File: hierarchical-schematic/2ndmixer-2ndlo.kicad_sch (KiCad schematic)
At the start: 58 parts

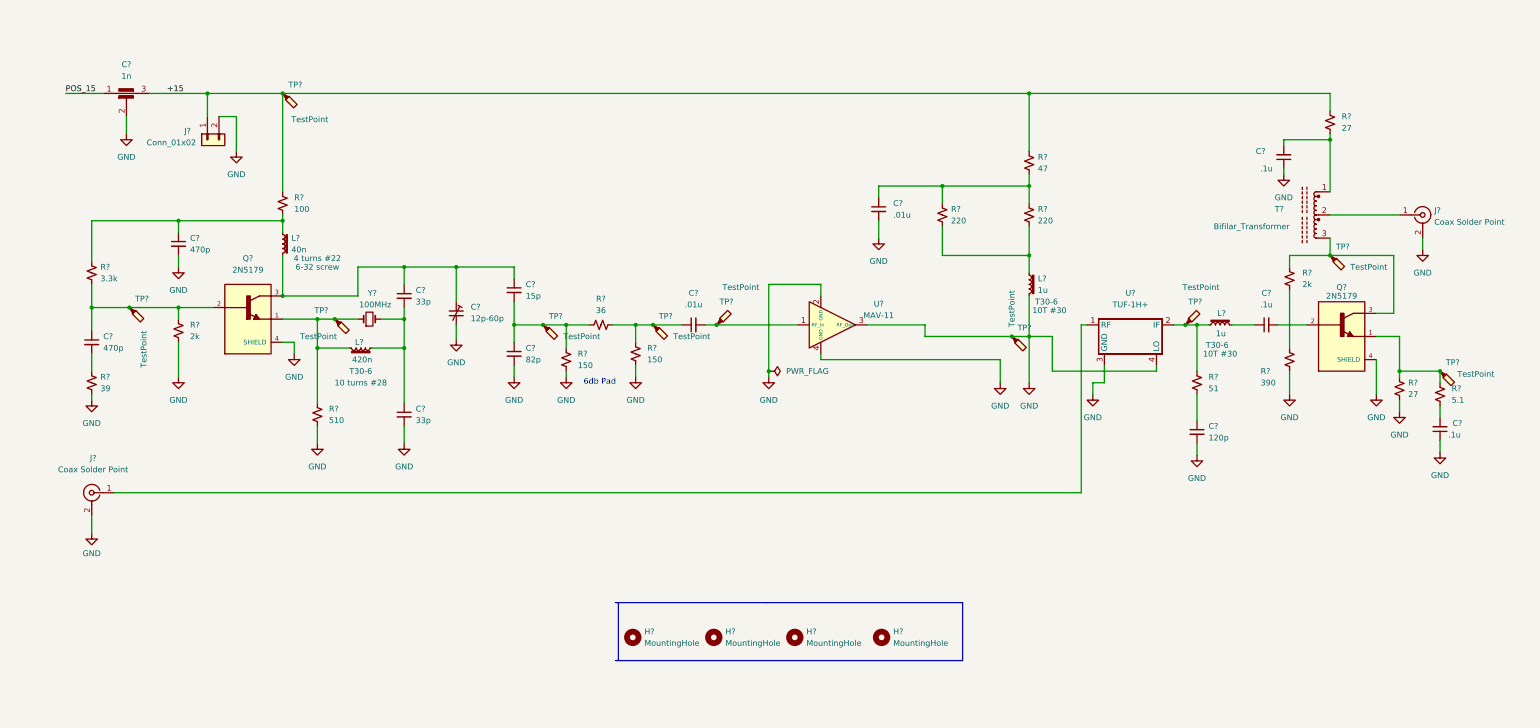
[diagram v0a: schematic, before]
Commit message: Hierarchical schematic updates
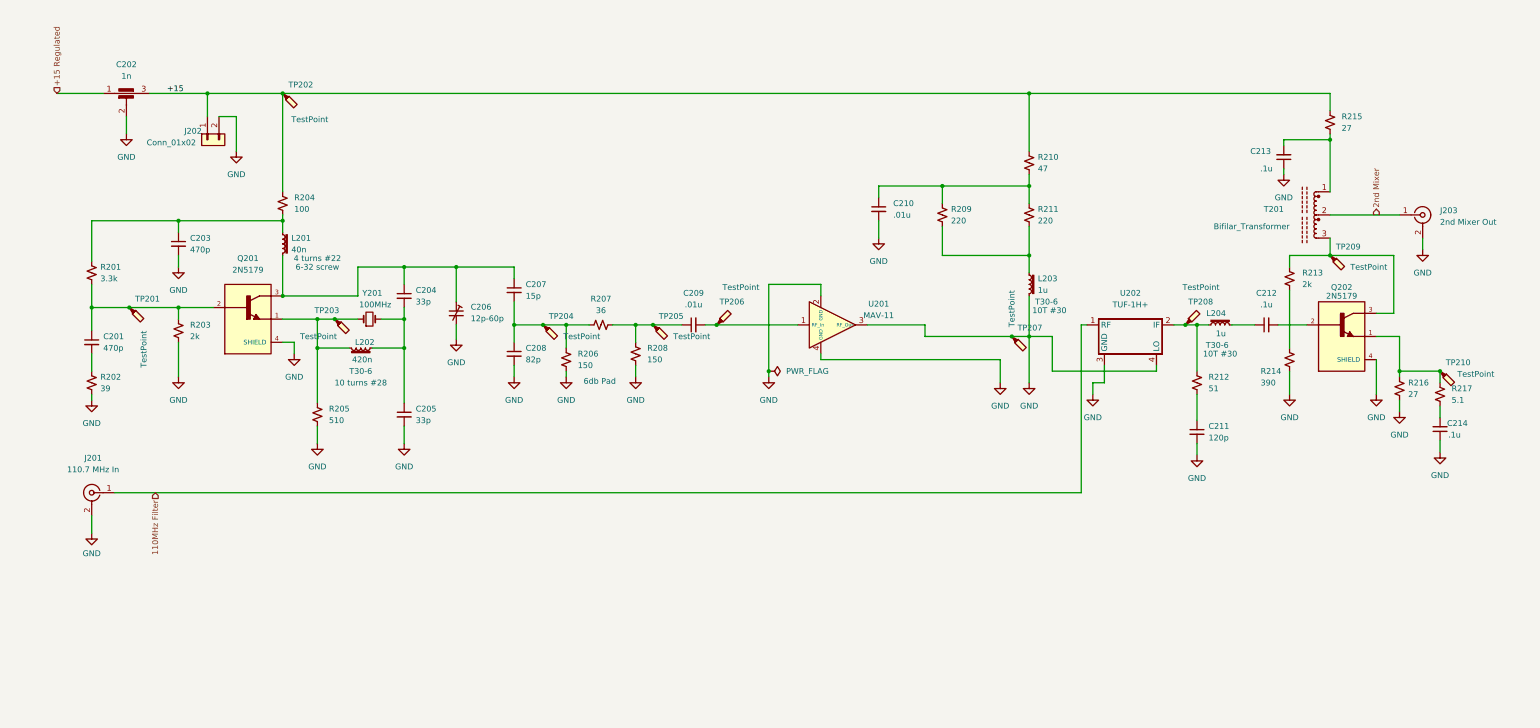
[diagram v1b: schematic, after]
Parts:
- removed H? (x4): MountingHole, MountingHole:MountingHole_3.2mm_M3, symbol Mechanical:MountingHole
- J201: renamed from J?; value Coax Solder Point -> 110.7 MHz In
- J203: renamed from J?; value Coax Solder Point -> 2nd Mixer Out
- gave numbers to parts that had none: 52
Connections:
- net 2nd Mixer: now reaches J203.1 (In), T201.2
- net 110MHz Filter: now reaches J201.1 (In), U202.1 (RF)
- net POS_15 renamed +15 Regulated
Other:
- company: (none) -> Andy McCann KA3KAF and Doug McCann KA3KAG

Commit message: hierarchical schematic updated to pass erc
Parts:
- Q201, Q202: footprint 2ndmixer-2ndlo:TO127P584H533-4N -> TO127P584H533-4N; symbol 2ndmixer-2ndlo:2N5179 -> spectrum analyzer:2N5179
- T201: symbol 2ndmixer-2ndlo:Bifilar_Transformer -> spectrum analyzer:Bifilar_Transformer
- U201: symbol 2ndmixer-2ndlo:MAV-11 -> spectrum analyzer:MAV-11
- U202: symbol 2ndmixer-2ndlo:TUF-1H+ -> spectrum analyzer:TUF-1H+
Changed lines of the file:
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@@
   (junction (at 232.41 41.91) (diameter 0) (color 0 0 0 0)
   )
-  (junction (at 175.26 102.87) (diameter 0) (color 0 0 0 0)
-  )
   (junction (at 322.58 102.87) (diameter 0) (color 0 0 0 0)
   )
@@
     (stroke (width 0) (type default) (color 0 0 0 0))
   )
-  (wire (pts (xy 175.26 83.82) (xy 175.26 102.87))
+  (wire (pts (xy 175.26 83.82) (xy 175.26 104.14))
     (stroke (width 0) (type default) (color 0 0 0 0))
   )
@@
   )
   (wire (pts (xy 232.41 62.23) (xy 232.41 59.69))
-    (stroke (width 0) (type default) (color 0 0 0 0))
-  )
-  (wire (pts (xy 175.26 102.87) (xy 175.26 104.14))
     (stroke (width 0) (type default) (color 0 0 0 0))
   )
@@
     (pin "1")
   )
-  (symbol (lib_id "2ndmixer-2ndlo:MAV-11") (at 186.69 92.71 0) (unit 1)
+  (symbol (lib_id "spectrum analyzer:MAV-11") (at 186.69 92.71 0) (unit 1)
     (in_bom yes) (on_board yes) (fields_autoplaced)
     (property "Reference" "U201" (id 0) (at 199.39 88.0933 0))
@@
     (pin "1")
   )
-  (symbol (lib_id "2ndmixer-2ndlo:Bifilar_Transformer") (at 292.1 68.58 270) (unit 1)
+  (symbol (lib_id "spectrum analyzer:Bifilar_Transformer") (at 292.1 68.58 270) (unit 1)
     (in_bom yes) (on_board yes)
     (property "Reference" "T201" (id 0) (at 288.29 67.31 90)
@@
       (effects (font (size 1.27 1.27)) (justify right))
     )
-    (property "Footprint" "Transformer_THT:Autotransformer_Toroid_1Tap_Horizontal_D10.5mm_Amidon-T37" (id 2) (at 292.1 68.58 0)
-      (effects (font (size 1.27 1.27)) hide)
-    )
-    (property "Datasheet" "" (id 3) (at 292.1 68.58 0)
+    (property "Footprint" "Transformer_THT:Autotransformer_Toroid_1Tap_Horizontal_D10.5mm_Amidon-T37" (id 2) (at 295.275 62.23 0)
+      (effects (font (size 1.27 1.27)) hide)
+    )
+    (property "Datasheet" "" (id 3) (at 295.275 62.23 0)
       (effects (font (size 1.27 1.27)) hide)
     )
@@
     (pin "1")
     (pin "2")
-  )
-  (symbol (lib_id "power:PWR_FLAG") (at 175.26 102.87 270) (unit 1)
-    (in_bom yes) (on_board yes) (fields_autoplaced)
-    (property "Reference" "#FLG0201" (id 0) (at 177.165 102.87 0)
-      (effects (font (size 1.27 1.27)) hide)
-    )
-    (property "Value" "PWR_FLAG" (id 1) (at 179.07 102.8699 90)
-      (effects (font (size 1.27 1.27)) (justify left))
-    )
-    (property "Footprint" "" (id 2) (at 175.26 102.87 0)
-      (effects (font (size 1.27 1.27)) hide)
-    )
-    (property "Datasheet" "~" (id 3) (at 175.26 102.87 0)
-      (effects (font (size 1.27 1.27)) hide)
-    )
-    (pin "1")
   )
   (symbol (lib_id "power:GND") (at 95.25 118.745 0) (unit 1)
@@
     (pin "1")
   )
-  (symbol (lib_id "2ndmixer-2ndlo:TUF-1H+") (at 254 95.25 0) (unit 1)
+  (symbol (lib_id "spectrum analyzer:TUF-1H+") (at 254 95.25 0) (unit 1)
     (in_bom yes) (on_board yes) (fields_autoplaced)
     (property "Reference" "U202" (id 0) (at 254.635 85.725 0))
@@
     (pin "2")
   )
-  (symbol (lib_id "2ndmixer-2ndlo:2N5179") (at 60.96 91.44 0) (unit 1)
+  (symbol (lib_id "spectrum analyzer:2N5179") (at 60.96 91.44 0) (unit 1)
     (in_bom yes) (on_board yes) (fields_autoplaced)
     (property "Reference" "Q201" (id 0) (at 60.96 78.105 0))
     (property "Value" "2N5179" (id 1) (at 60.96 80.645 0))
-    (property "Footprint" "2ndmixer-2ndlo:TO127P584H533-4N" (id 2) (at 60.96 91.44 0)
+    (property "Footprint" "TO127P584H533-4N" (id 2) (at 60.96 91.44 0)
       (effects (font (size 1.27 1.27)) (justify left bottom) hide)
     )
@@
     (pin "2")
   )
-  (symbol (lib_id "2ndmixer-2ndlo:2N5179") (at 300.99 95.25 0) (unit 1)
+  (symbol (lib_id "spectrum analyzer:2N5179") (at 300.99 95.25 0) (unit 1)
     (in_bom yes) (on_board yes)
     (property "Reference" "Q202" (id 0) (at 300.99 84.455 0))
     (property "Value" "2N5179" (id 1) (at 300.99 86.36 0))
-    (property "Footprint" "2ndmixer-2ndlo:TO127P584H533-4N" (id 2) (at 300.99 95.25 0)
+    (property "Footprint" "TO127P584H533-4N" (id 2) (at 300.99 95.25 0)
       (effects (font (size 1.27 1.27)) (justify left bottom) hide)
     )

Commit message: appearance improvements
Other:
- moved on the sheet: L204
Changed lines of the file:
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@@
   (junction (at 95.25 80.01) (diameter 0) (color 0 0 0 0)
   )
+  (junction (at 298.45 53.34) (diameter 0) (color 0 0 0 0)
+  )
+  (junction (at 313.69 68.58) (diameter 0) (color 0 0 0 0)
+  )
   (junction (at 232.41 95.25) (diameter 0) (color 0 0 0 0)
   )
@@
   (junction (at 266.7 92.71) (diameter 0) (color 0 0 0 0)
   )
+  (junction (at 31.75 129.54) (diameter 0) (color 0 0 0 0)
+  )
   (junction (at 95.25 91.44) (diameter 0) (color 0 0 0 0)
   )
   (junction (at 232.41 77.47) (diameter 0) (color 0 0 0 0)
   )
-  (junction (at 298.45 52.07) (diameter 0) (color 0 0 0 0)
-  )
   (junction (at 146.05 92.71) (diameter 0) (color 0 0 0 0)
   )
@@
     (stroke (width 0) (type default) (color 0 0 0 0))
   )
+  (wire (pts (xy 313.69 60.325) (xy 313.69 68.58))
+    (stroke (width 0) (type default) (color 0 0 0 0))
+  )
   (wire (pts (xy 119.38 92.71) (xy 119.38 96.52))
     (stroke (width 0) (type default) (color 0 0 0 0))
@@
     (stroke (width 0) (type default) (color 0 0 0 0))
   )
+  (wire (pts (xy 26.67 117.475) (xy 31.75 117.475))
+    (stroke (width 0) (type default) (color 0 0 0 0))
+  )
   (wire (pts (xy 322.58 105.41) (xy 322.58 102.87))
     (stroke (width 0) (type default) (color 0 0 0 0))
@@
     (stroke (width 0) (type default) (color 0 0 0 0))
   )
-  (wire (pts (xy 298.45 52.07) (xy 298.45 63.5))
+  (wire (pts (xy 298.45 50.8) (xy 298.45 53.34))
     (stroke (width 0) (type default) (color 0 0 0 0))
   )
@@
     (stroke (width 0) (type default) (color 0 0 0 0))
   )
+  (wire (pts (xy 31.75 117.475) (xy 31.75 129.54))
+    (stroke (width 0) (type default) (color 0 0 0 0))
+  )
   (wire (pts (xy 313.69 102.87) (xy 313.69 104.14))
     (stroke (width 0) (type default) (color 0 0 0 0))
@@
     (stroke (width 0) (type default) (color 0 0 0 0))
   )
+  (wire (pts (xy 298.45 53.34) (xy 298.45 63.5))
+    (stroke (width 0) (type default) (color 0 0 0 0))
+  )
   (wire (pts (xy 232.41 95.25) (xy 237.49 95.25))
     (stroke (width 0) (type default) (color 0 0 0 0))
@@
     (stroke (width 0) (type default) (color 0 0 0 0))
   )
-  (wire (pts (xy 288.29 52.07) (xy 298.45 52.07))
+  (wire (pts (xy 288.29 53.34) (xy 298.45 53.34))
     (stroke (width 0) (type default) (color 0 0 0 0))
   )
@@
     (stroke (width 0) (type default) (color 0 0 0 0))
   )
-  (wire (pts (xy 298.45 50.8) (xy 298.45 52.07))
-    (stroke (width 0) (type default) (color 0 0 0 0))
-  )
   (wire (pts (xy 95.25 109.855) (xy 95.25 97.79))
     (stroke (width 0) (type default) (color 0 0 0 0))
@@
     (stroke (width 0) (type default) (color 0 0 0 0))
   )
+  (wire (pts (xy 318.77 60.325) (xy 313.69 60.325))
+    (stroke (width 0) (type default) (color 0 0 0 0))
+  )
   (wire (pts (xy 146.05 92.71) (xy 140.97 92.71))
     (stroke (width 0) (type default) (color 0 0 0 0))
@@
     (stroke (width 0) (type default) (color 0 0 0 0))
   )
-  (wire (pts (xy 281.94 92.71) (xy 276.86 92.71))
+  (wire (pts (xy 281.94 92.71) (xy 278.892 92.71))
     (stroke (width 0) (type default) (color 0 0 0 0))
   )
@@
     (stroke (width 0) (type default) (color 0 0 0 0))
   )
-  (wire (pts (xy 288.29 53.34) (xy 288.29 52.07))
-    (stroke (width 0) (type default) (color 0 0 0 0))
-  )
   (wire (pts (xy 209.55 92.71) (xy 209.55 95.25))
     (stroke (width 0) (type default) (color 0 0 0 0))
@@
     (stroke (width 0) (type default) (color 0 0 0 0))
   )
-  (wire (pts (xy 269.24 92.71) (xy 271.78 92.71))
+  (wire (pts (xy 269.24 92.71) (xy 273.812 92.71))
     (stroke (width 0) (type default) (color 0 0 0 0))
   )
@@
     (effects (font (size 1.27 1.27)) (justify left bottom))
   )
-  (hierarchical_label "2nd Mixer" (shape output) (at 308.61 68.58 90)
+  (hierarchical_label "2nd Mixer" (shape output) (at 318.77 60.325 0)
     (effects (font (size 1.27 1.27)) (justify left))
   )
@@
     (effects (font (size 1.27 1.27)) (justify left))
   )
-  (hierarchical_label "110MHz Filter" (shape input) (at 40.64 129.54 270)
+  (hierarchical_label "110MHz Filter" (shape input) (at 26.67 117.475 180)
     (effects (font (size 1.27 1.27)) (justify right))
   )
@@
     (pin "1")
   )
-  (symbol (lib_id "Device:L_Iron_Small") (at 274.32 92.71 90) (unit 1)
-    (in_bom yes) (on_board yes)
-    (property "Reference" "L204" (id 0) (at 275.59 90.17 90)
-      (effects (font (size 1.27 1.27)) (justify left))
-    )
-    (property "Value" "1u" (id 1) (at 275.59 94.615 90)
-      (effects (font (size 1.27 1.27)) (justify left))
-    )
-    (property "Footprint" "Inductor_THT:L_Toroid_Vertical_L13.0mm_W6.5mm_P5.60mm" (id 2) (at 274.32 92.71 0)
-      (effects (font (size 1.27 1.27)) hide)
-    )
-    (property "Datasheet" "~" (id 3) (at 274.32 92.71 0)
-      (effects (font (size 1.27 1.27)) hide)
-    )
-    (property "Field4" "T30-6" (id 4) (at 273.685 97.155 90))
-    (property "Field5" "10T #30" (id 5) (at 274.32 99.06 90))
+  (symbol (lib_id "Device:L_Iron_Small") (at 276.352 92.71 90) (unit 1)
+    (in_bom yes) (on_board yes)
+    (property "Reference" "L204" (id 0) (at 277.622 90.17 90)
+      (effects (font (size 1.27 1.27)) (justify left))
+    )
+    (property "Value" "1u" (id 1) (at 277.622 94.615 90)
+      (effects (font (size 1.27 1.27)) (justify left))
+    )
+    (property "Footprint" "Inductor_THT:L_Toroid_Vertical_L13.0mm_W6.5mm_P5.60mm" (id 2) (at 276.352 92.71 0)
+      (effects (font (size 1.27 1.27)) hide)
+    )
+    (property "Datasheet" "~" (id 3) (at 276.352 92.71 0)
+      (effects (font (size 1.27 1.27)) hide)
+    )
+    (property "Field4" "T30-6" (id 4) (at 275.717 97.155 90))
+    (property "Field5" "10T #30" (id 5) (at 276.352 99.06 90))
     (pin "1")
     (pin "2")
@@
   )
   (symbol (lib_id "Connector:Conn_Coaxial") (at 26.67 129.54 0) (mirror y) (unit 1)
-    (in_bom yes) (on_board yes) (fields_autoplaced)
-    (property "Reference" "J201" (id 0) (at 26.9874 121.92 0))
-    (property "Value" "110.7 MHz In" (id 1) (at 26.9874 124.46 0))
+    (in_bom yes) (on_board yes)
+    (property "Reference" "J201" (id 0) (at 24.384 124.206 0))
+    (property "Value" "110.7 MHz In" (id 1) (at 24.13 126.365 0))
     (property "Footprint" "Connector_Wire:SolderWire-0.5sqmm_1x02_P4.6mm_D0.9mm_OD2.1mm" (id 2) (at 26.67 129.54 0)
       (effects (font (size 1.27 1.27)) hide)
